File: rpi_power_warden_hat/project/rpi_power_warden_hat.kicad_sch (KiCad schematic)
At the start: 2 parts, among them J2 Conn_01x04, J4 Conn_01x04

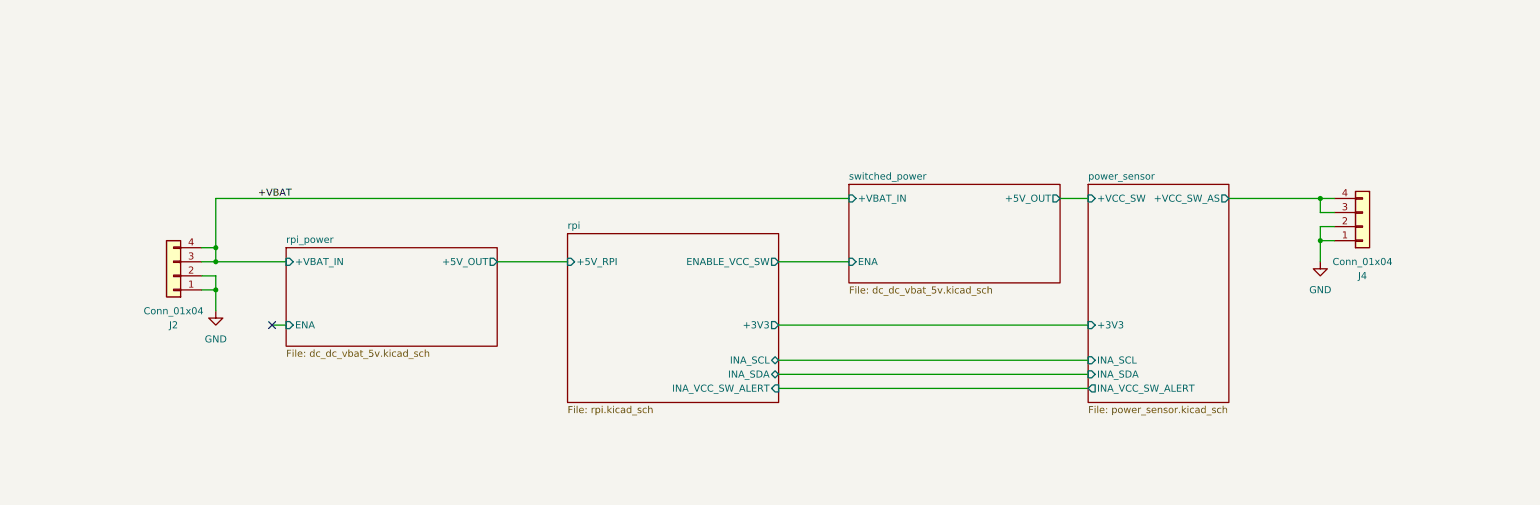
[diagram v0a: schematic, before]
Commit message: feat: put USB A receptacle to deliver power, have progress in INA260 and place test poitns
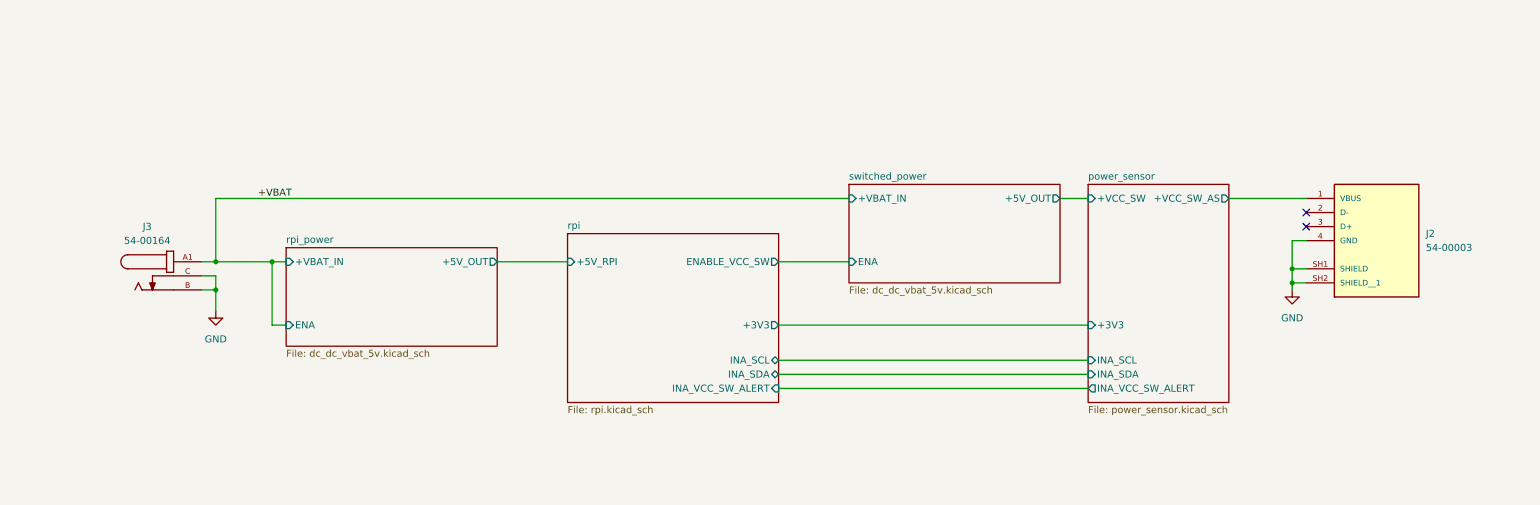
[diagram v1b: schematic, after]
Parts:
- removed J2, J4: Conn_01x04, symbol Connector_Generic:Conn_01x04
- added J2: 54-00003, rpi_power_warden_hat:TENSILITY_54-00003, symbol rpi_power_warden_hat:54-00003
- added J3: 54-00164, rpi_power_warden_hat:TENSILITY_54-00164, symbol rpi_power_warden_hat:54-00164
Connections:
- net +VBAT: now also J3.A1, J3.A2
- net GND: now also J2.4 (GND), J2.SH1 (SHIELD), J2.SH2 (SHIELD__1), J3.B, J3.C
- net power_sensor/+VCC_SW_AS: now also J2.1 (VBUS)
- no-connect marks 1 -> 2

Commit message: add a switched vbat feature
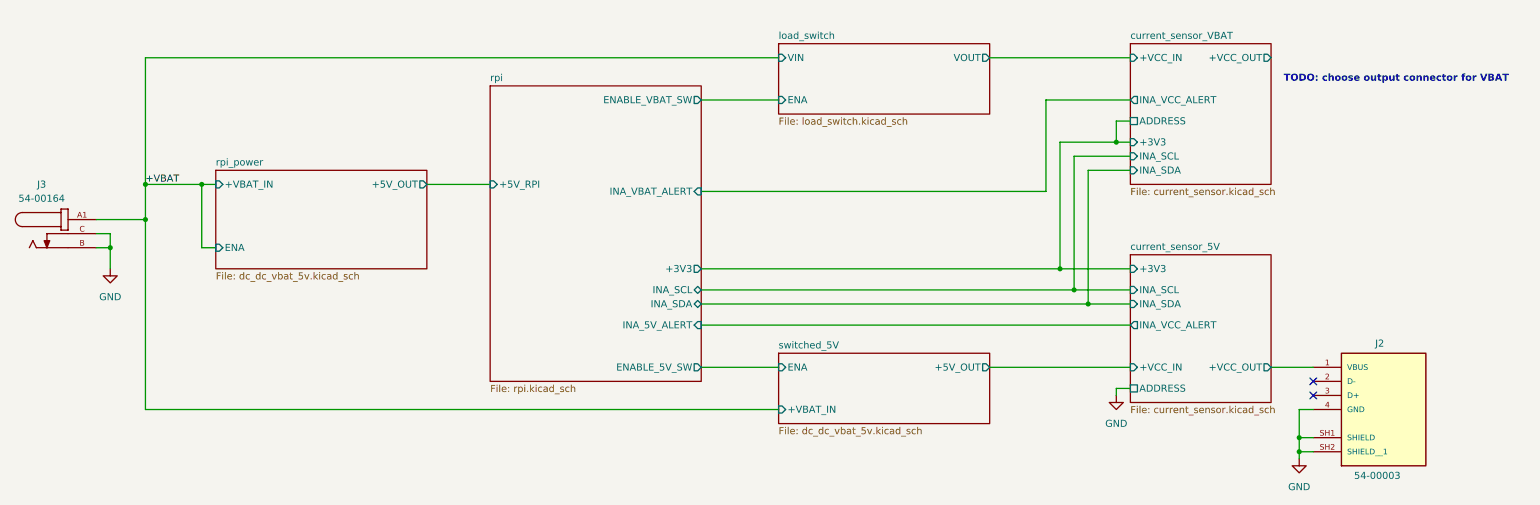
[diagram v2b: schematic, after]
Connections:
- net current_sensor_5V/+VCC_SW_AS renamed current_sensor_5V/+VCC_OUT
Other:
- sheet power_sensor renamed current_sensor_5V
- sheet switched_power renamed switched_5V
- added sheet current_sensor_VBAT (current_sensor.kicad_sch)
- added sheet load_switch (load_switch.kicad_sch)
- sheet current_sensor_5V: file power_sensor.kicad_sch -> current_sensor.kicad_sch
- sheet current_sensor_5V ports: added +VCC_IN, +VCC_OUT, ADDRESS, INA_VCC_ALERT; removed +VCC_SW, +VCC_SW_AS, INA_VCC_SW_ALERT
- sheet rpi ports: added ENABLE_5V_SW, ENABLE_VBAT_SW, INA_5V_ALERT, INA_VBAT_ALERT; removed ENABLE_VCC_SW, INA_VCC_SW_ALERT
- note added: "TODO: choose output connector for VBAT"
- moved on the sheet: J2

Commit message: re-annotate schematic, add leds to power supply outputs and add connector for VBAT switched load
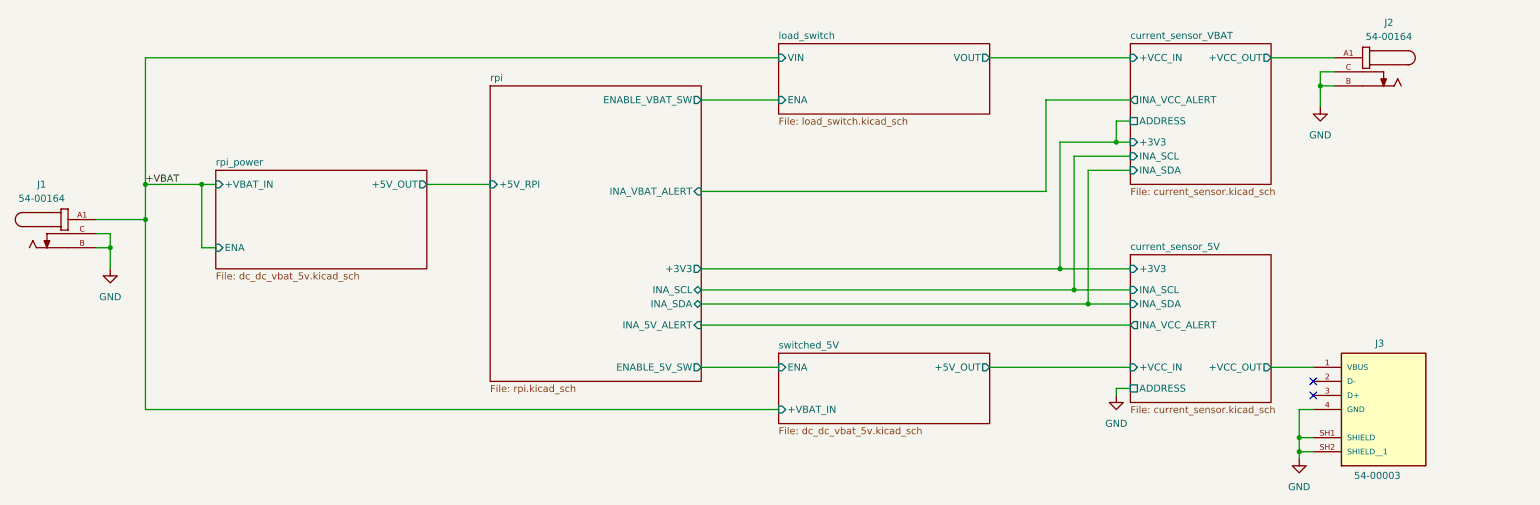
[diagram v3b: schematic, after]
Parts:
- added J2: 54-00164, rpi_power_warden_hat:TENSILITY_54-00164, symbol rpi_power_warden_hat:54-00164
- renumbered J3 to J1, J2 to J3
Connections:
- net GND: now also J2.B, J2.C
- net current_sensor_VBAT/+VCC_OUT: now also J2.A1, J2.A2
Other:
- note removed: "TODO: choose output connector for VBAT"
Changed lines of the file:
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@@
+	)
+	(junction
+		(at 250.19 45.72)
+		(diameter 0)
+		(color 0 0 0 0)
 	)
 	(junction
@@
 	(wire
 		(pts
+			(xy 241.3 40.64) (xy 252.73 40.64)
+		)
+		(stroke
+			(width 0)
+			(type default)
+		)
+	)
+	(wire
+		(pts
 			(xy 203.2 78.74) (xy 215.9 78.74)
 		)
@@
 	(wire
 		(pts
+			(xy 250.19 43.18) (xy 250.19 45.72)
+		)
+		(stroke
+			(width 0)
+			(type default)
+		)
+	)
+	(wire
+		(pts
 			(xy 213.36 100.33) (xy 213.36 101.6)
 		)
@@
 	(wire
 		(pts
+			(xy 252.73 45.72) (xy 250.19 45.72)
+		)
+		(stroke
+			(width 0)
+			(type default)
+		)
+	)
+	(wire
+		(pts
 			(xy 203.2 55.88) (xy 203.2 78.74)
 		)
@@
 	(wire
 		(pts
+			(xy 252.73 43.18) (xy 250.19 43.18)
+		)
+		(stroke
+			(width 0)
+			(type default)
+		)
+	)
+	(wire
+		(pts
 			(xy 29.21 72.39) (xy 31.75 72.39)
 		)
@@
 	(wire
 		(pts
+			(xy 250.19 49.53) (xy 250.19 45.72)
+		)
+		(stroke
+			(width 0)
+			(type default)
+		)
+	)
+	(wire
+		(pts
 			(xy 215.9 55.88) (xy 213.36 55.88)
 		)
@@
 			(width 0)
 			(type default)
-		)
-	)
-	(text "TODO: choose output connector for VBAT\n"
-		(exclude_from_sim no)
-		(at 263.906 44.45 0)
-		(effects
-			(font
-				(size 1.27 1.27)
-				(thickness 0.254)
-				(bold yes)
-			)
 		)
 	)
@@
 		(on_board yes)
 		(dnp no)
-		(property "Reference" "J2"
+		(property "Reference" "J3"
 			(at 260.096 92.202 0)
 			(effects
@@
 			(project ""
 				(path "/8692c5de-a943-41e8-8e29-f6c5e99cda34"
-					(reference "J2")
+					(reference "J3")
 					(unit 1)
 				)
@@
 		(dnp no)
 		(fields_autoplaced yes)
-		(property "Reference" "#PWR21"
+		(property "Reference" "#PWR2"
 			(at 213.36 107.95 0)
 			(effects
@@
 			(project "rpi_power_warden_hat"
 				(path "/8692c5de-a943-41e8-8e29-f6c5e99cda34"
-					(reference "#PWR21")
+					(reference "#PWR2")
+					(unit 1)
+				)
+			)
+		)
+	)
+	(symbol
+		(lib_id "rpi_power_warden_hat:54-00164")
+		(at 257.81 43.18 0)
+		(mirror y)
+		(unit 1)
+		(exclude_from_sim no)
+		(in_bom yes)
+		(on_board yes)
+		(dnp no)
+		(property "Reference" "J2"
+			(at 262.5697 34.29 0)
+			(effects
+				(font
+					(size 1.27 1.27)
+				)
+			)
+		)
+		(property "Value" "54-00164"
+			(at 262.5697 36.83 0)
+			(effects
+				(font
+					(size 1.27 1.27)
+				)
+			)
+		)
+		(property "Footprint" "rpi_power_warden_hat:TENSILITY_54-00164"
+			(at 254.762 30.226 0)
+			(effects
+				(font
+					(size 1.27 1.27)
+				)
+				(justify bottom)
+				(hide yes)
+			)
+		)
+		(property "Datasheet" "https://tensility.s3.us-west-2.amazonaws.com/uploads/pdffiles/54-00164.pdf"
+			(at 254.762 30.226 0)
+			(effects
+				(font
+					(size 1.27 1.27)
+				)
+				(hide yes)
+			)
+		)
+		(property "Description" "CONN JACK R/A SMT 5.5X2.1MM"
+			(at 257.048 32.766 0)
+			(effects
+				(font
+					(size 1.27 1.27)
+				)
+				(hide yes)
+			)
+		)
+		(property "mpn" "54-00164"
+			(at 258.826 35.052 0)
+			(effects
+				(font
+					(size 1.27 1.27)
+				)
+				(justify bottom)
+				(hide yes)
+			)
+		)
+		(property "manufacturer" "TENSILITY"
+			(at 256.794 34.544 0)
+			(effects
+				(font
+					(size 1.27 1.27)
+				)
+				(justify bottom)
+				(hide yes)
+			)
+		)
+		(pin "A2"
+		)
+		(pin "B"
+		)
+		(pin "C"
+		)
+		(pin "A1"
+		)
+		(instances
+			(project "rpi_power_warden_hat"
+				(path "/8692c5de-a943-41e8-8e29-f6c5e99cda34"
+					(reference "J2")
+					(unit 1)
+				)
+			)
+		)
+	)
+	(symbol
+		(lib_id "power:GND")
+		(at 250.19 49.53 0)
+		(mirror y)
+		(unit 1)
+		(exclude_from_sim no)
+		(in_bom yes)
+		(on_board yes)
+		(dnp no)
+		(fields_autoplaced yes)
+		(property "Reference" "#PWR4"
+			(at 250.19 55.88 0)
+			(effects
+				(font
+					(size 1.27 1.27)
+				)
+				(hide yes)
+			)
+		)
+		(property "Value" "GND"
+			(at 250.19 54.61 0)
+			(effects
+				(font
+					(size 1.27 1.27)
+				)
+			)
+		)
+		(property "Footprint" ""
+			(at 250.19 49.53 0)
+			(effects
+				(font
+					(size 1.27 1.27)
+				)
+				(hide yes)
+			)
+		)
+		(property "Datasheet" ""
+			(at 250.19 49.53 0)
+			(effects
+				(font
+					(size 1.27 1.27)
+				)
+				(hide yes)
+			)
+		)
+		(property "Description" "Power symbol creates a global label with name \"GND\" , ground"
+			(at 250.19 49.53 0)
+			(effects
+				(font
+					(size 1.27 1.27)
+				)
+				(hide yes)
+			)
+		)
+		(pin "1"
+		)
+		(instances
+			(project "rpi_power_warden_hat"
+				(path "/8692c5de-a943-41e8-8e29-f6c5e99cda34"
+					(reference "#PWR4")
 					(unit 1)
 				)
@@
 		(dnp no)
 		(fields_autoplaced yes)
-		(property "Reference" "J3"
+		(property "Reference" "J1"
 			(at 19.3703 63.5 0)
 			(effects
@@
 			(project "rpi_power_warden_hat"
 				(path "/8692c5de-a943-41e8-8e29-f6c5e99cda34"
-					(reference "J3")
+					(reference "J1")
 					(unit 1)
 				)
@@
 		(dnp no)
 		(fields_autoplaced yes)
-		(property "Reference" "#PWR2"
+		(property "Reference" "#PWR3"
 			(at 246.38 119.38 0)
 			(effects
@@
 			(project "rpi_power_warden_hat"
 				(path "/8692c5de-a943-41e8-8e29-f6c5e99cda34"
-					(reference "#PWR2")
+					(reference "#PWR3")
 					(unit 1)
 				)

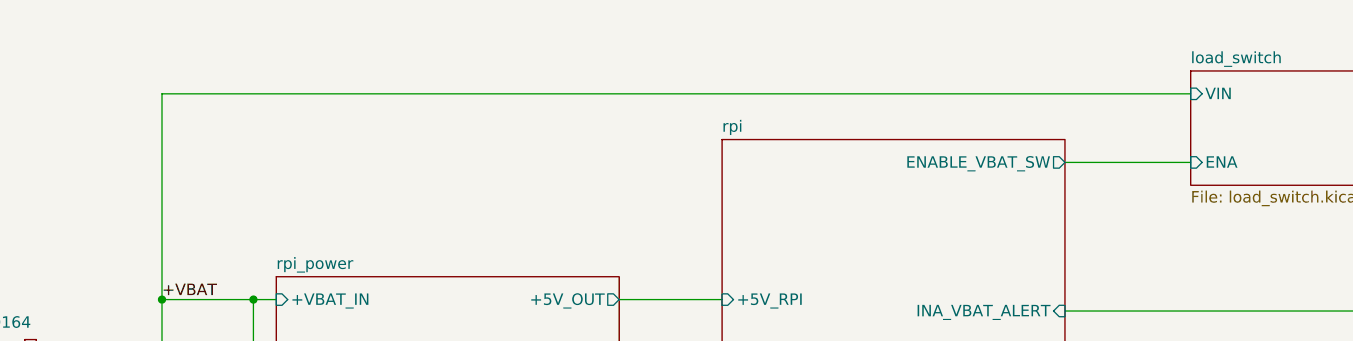
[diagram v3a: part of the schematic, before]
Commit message: add RPi HAT eeprom to schematic
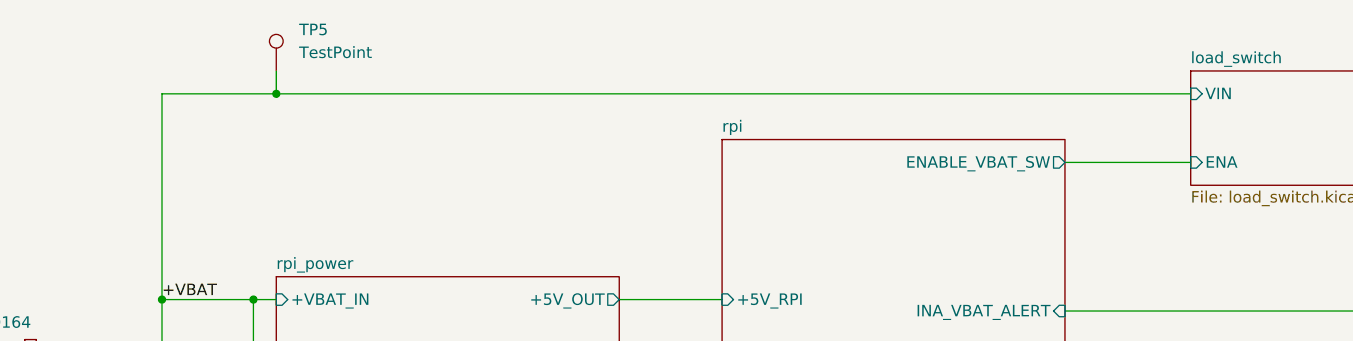
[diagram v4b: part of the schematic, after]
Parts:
- added TP5: TestPoint, TestPoint:TestPoint_Pad_D2.5mm, symbol Connector:TestPoint
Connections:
- net +VBAT: now also TP5.1
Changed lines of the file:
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@@
+	)
+	(junction
+		(at 50.8 40.64)
+		(diameter 0)
+		(color 0 0 0 0)
 	)
 	(junction
@@
 	(wire
 		(pts
+			(xy 50.8 38.1) (xy 50.8 40.64)
+		)
+		(stroke
+			(width 0)
+			(type default)
+		)
+	)
+	(wire
+		(pts
 			(xy 246.38 109.22) (xy 246.38 111.76)
 		)
@@
 	(wire
 		(pts
+			(xy 50.8 40.64) (xy 152.4 40.64)
+		)
+		(stroke
+			(width 0)
+			(type default)
+		)
+	)
+	(wire
+		(pts
 			(xy 48.26 63.5) (xy 48.26 74.93)
 		)
@@
 	(wire
 		(pts
-			(xy 152.4 40.64) (xy 38.1 40.64)
+			(xy 38.1 40.64) (xy 50.8 40.64)
 		)
 		(stroke
@@
 					(unit 1)
 				)
+			)
+		)
+	)
+	(symbol
+		(lib_id "Connector:TestPoint")
+		(at 50.8 38.1 0)
+		(unit 1)
+		(exclude_from_sim no)
+		(in_bom yes)
+		(on_board yes)
+		(dnp no)
+		(fields_autoplaced yes)
+		(property "Reference" "TP5"
+			(at 53.34 33.5279 0)
+			(effects
+				(font
+					(size 1.27 1.27)
+				)
+				(justify left)
+			)
+		)
+		(property "Value" "TestPoint"
+			(at 53.34 36.0679 0)
+			(effects
+				(font
+					(size 1.27 1.27)
+				)
+				(justify left)
+			)
+		)
+		(property "Footprint" "TestPoint:TestPoint_Pad_D2.5mm"
+			(at 55.88 38.1 0)
+			(effects
+				(font
+					(size 1.27 1.27)
+				)
+				(hide yes)
+			)
+		)
+		(property "Datasheet" "~"
+			(at 55.88 38.1 0)
+			(effects
+				(font
+					(size 1.27 1.27)
+				)
+				(hide yes)
+			)
+		)
+		(property "Description" "test point"
+			(at 50.8 38.1 0)
+			(effects
+				(font
+					(size 1.27 1.27)
+				)
+				(hide yes)
+			)
+		)
+		(pin "1"
+		)
+		(instances
+			(project "rpi_power_warden_hat"
+				(path "/8692c5de-a943-41e8-8e29-f6c5e99cda34"
+					(reference "TP5")
+					(unit 1)
+				)

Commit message: re-annotate schematic
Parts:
- renumbered TP5 to TP1
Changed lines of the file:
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@@
 		(dnp no)
 		(fields_autoplaced yes)
-		(property "Reference" "TP5"
+		(property "Reference" "TP1"
 			(at 53.34 33.5279 0)
 			(effects
@@
 			(project "rpi_power_warden_hat"
 				(path "/8692c5de-a943-41e8-8e29-f6c5e99cda34"
-					(reference "TP5")
+					(reference "TP1")
 					(unit 1)
 				)

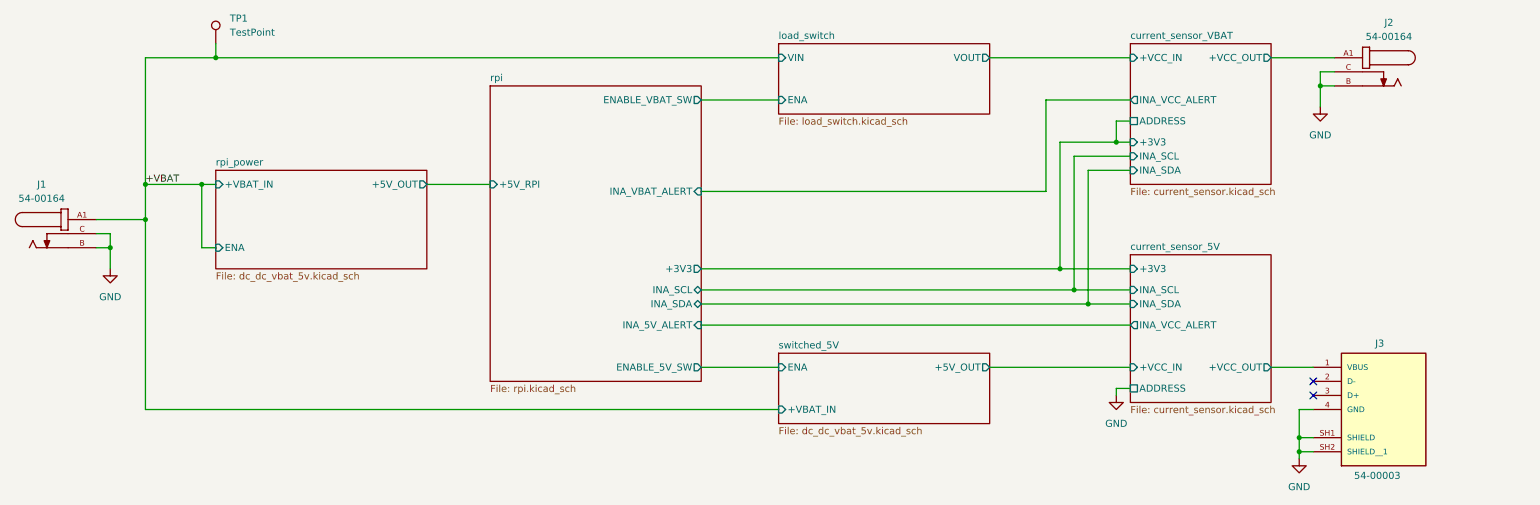
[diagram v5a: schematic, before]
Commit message: add and gate in swiched power supplies enable
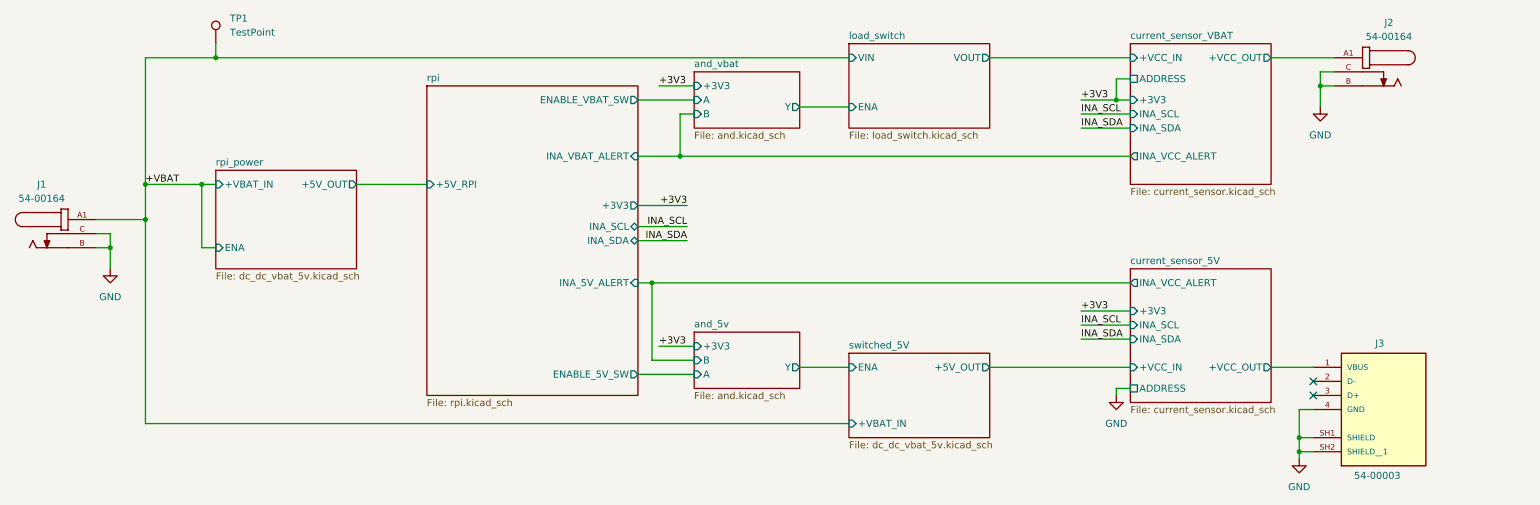
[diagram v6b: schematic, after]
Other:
- added sheet and_5v (and.kicad_sch)
- added sheet and_vbat (and.kicad_sch)
